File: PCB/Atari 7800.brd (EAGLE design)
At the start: 58.5 x 61 mm, 28 parts, among them U1A SN74AHCT125N, U2A SN74AHCT125N, U3A SN74AHCT125N, U4 CD74HC4053E, U5 CD74HC4053E

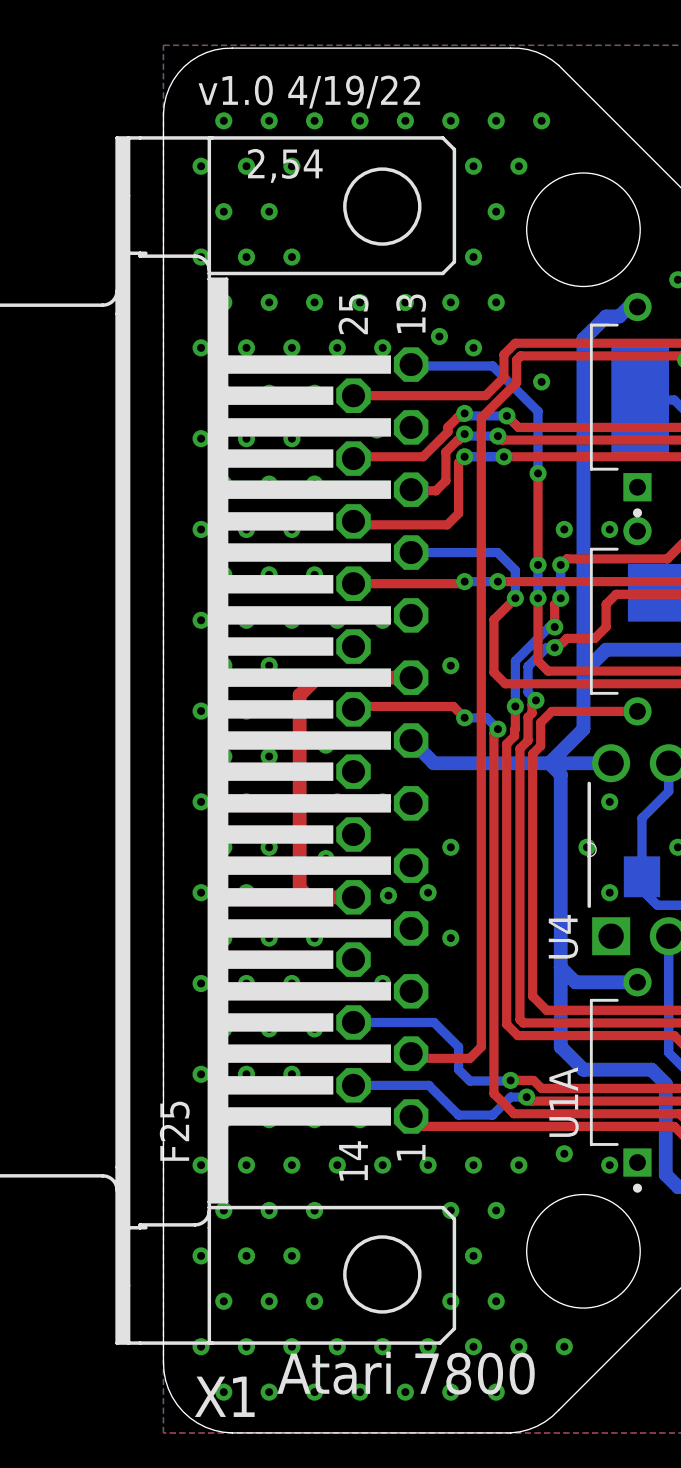
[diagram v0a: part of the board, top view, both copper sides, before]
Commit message: Added exposed GND plane at DB25 anchors
All PCBs have been update to have exposed GND plane pads for the DB25 anchor points.

This resolves Issue 54
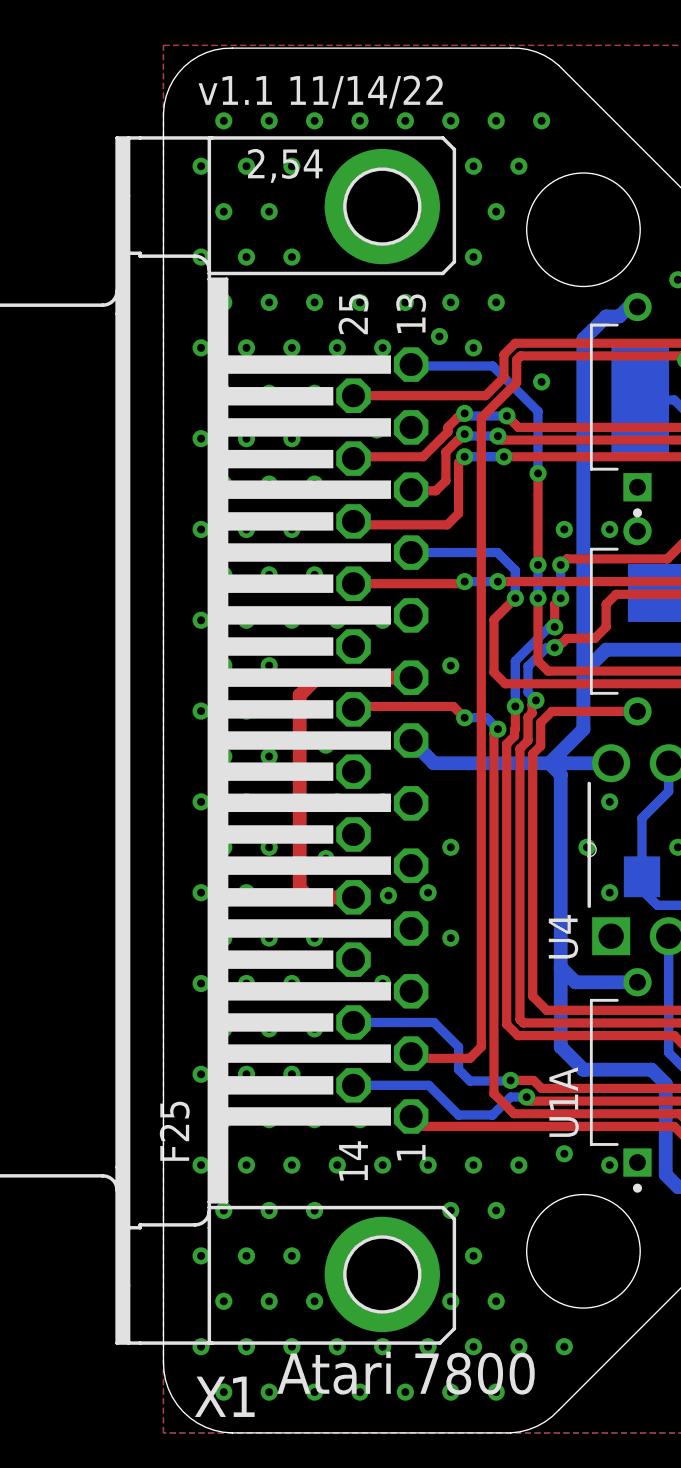
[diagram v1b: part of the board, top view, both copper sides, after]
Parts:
- X1: device SparkFun-Retired:F25H -> SparkFun-Retired:F25HP
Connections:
- net GND: now also X1.GND1, X1.GND2
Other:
- board text added: "v1.1 11/14/22"
- board text removed: "v1.0 4/19/22"
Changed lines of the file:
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@@
 <drawing>
 <settings>
-<setting alwaysvectorfont="yes"/>
+<setting alwaysvectorfont="no"/>
 <setting verticaltext="up"/>
 </settings>
@@
 <hole x="18.5" y="53" drill="5"/>
 <hole x="18.5" y="8" drill="5"/>
-<text x="1.5" y="58.5" size="1.27" layer="21">v1.0 4/19/22</text>
+<text x="1.5" y="58.5" size="1.27" layer="21">v1.1 11/14/22</text>
 <text x="16.5" y="3.5" size="1.778" layer="21" rot="R180">Atari 7800</text>
 <wire x1="58.5" y1="46.377359375" x2="58.5" y2="43.5" width="0" layer="20"/>
@@
 <attribute name="PURCHASE-URL" value="https://pricing.snapeda.com/search/part/SN74AHCT125N/?ref=eda" x="149.15" y="56.521" size="1.778" layer="27" rot="R90" display="off"/>
 </element>
-<element name="X1" library="SparkFun-Retired" package="F25H" value="" x="9.64" y="30.5" smashed="yes" rot="R90">
+<element name="X1" library="SparkFun-Retired" package="F25HP" value="" x="9.64" y="30.5" smashed="yes" rot="R90">
 <attribute name="NAME" x="4.219" y="2.48" size="1.778" layer="25" ratio="10" rot="R180"/>
 <attribute name="VALUE" x="-4.33" y="22.118" size="1.778" layer="27" ratio="10" rot="R90"/>
@@
 <contactref element="U2A" pad="13"/>
 <contactref element="U2A" pad="1"/>
-<contactref element="X1" pad="3"/>
-<contactref element="X1" pad="6"/>
-<contactref element="X1" pad="5"/>
-<contactref element="X1" pad="4"/>
-<contactref element="X1" pad="9"/>
 <contactref element="GND1" pad="1"/>
 <contactref element="GND2" pad="1"/>
-<contactref element="X1" pad="16"/>
 <contactref element="U4" pad="7"/>
 <contactref element="U4" pad="8"/>
@@
 <via x="54.6568" y="17.7968" extent="1-16" drill="0.35"/>
 <via x="56.6568" y="17.7968" extent="1-16" drill="0.35"/>
+<contactref element="X1" pad="3"/>
+<contactref element="X1" pad="6"/>
+<contactref element="X1" pad="5"/>
+<contactref element="X1" pad="4"/>
+<contactref element="X1" pad="9"/>
+<contactref element="X1" pad="16"/>
+<contactref element="X1" pad="GND2"/>
+<contactref element="X1" pad="GND1"/>
 </signal>
 <signal name="5VIN">

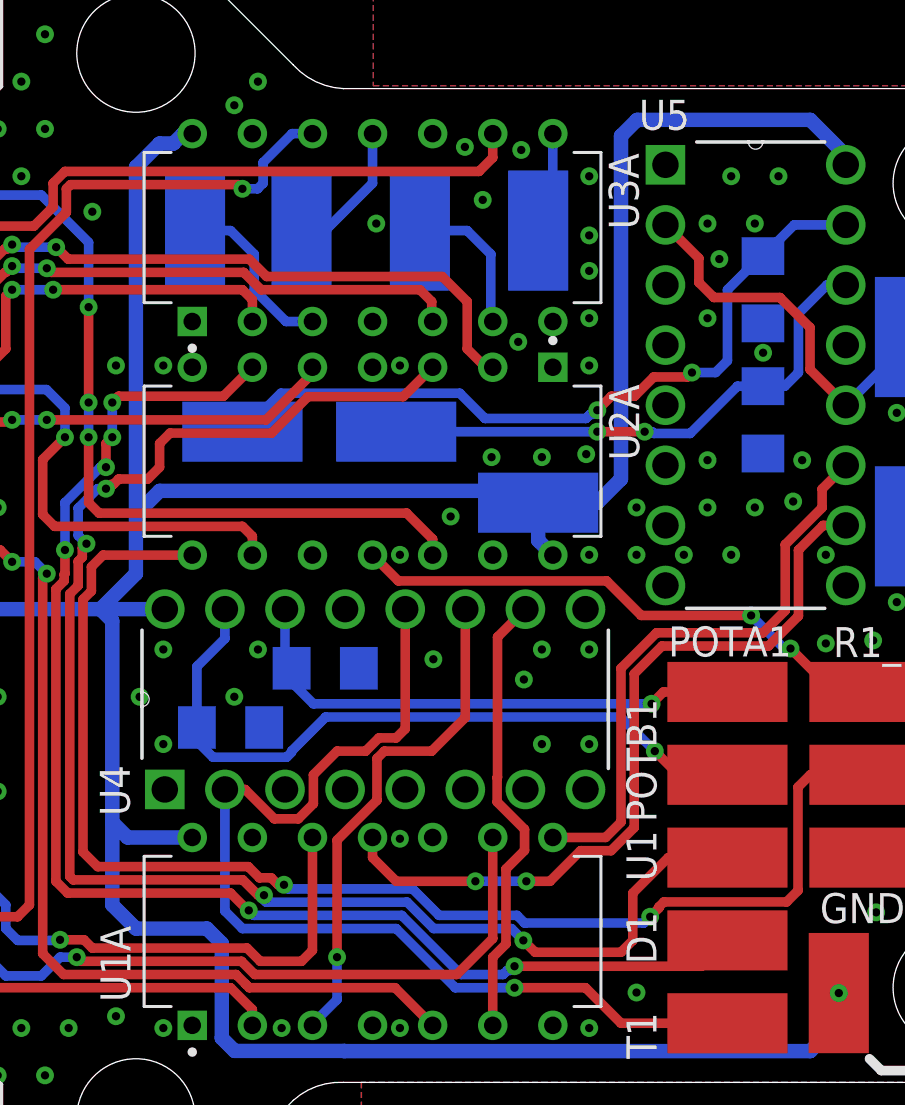
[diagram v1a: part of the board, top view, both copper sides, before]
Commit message: Silkscreen Update, Library Add, Datasheet Add
Updated the silkscreen on all PCBs that used the SN74 components as there was not orientation marker on the silkscreen.

Added Modified SN74 libraries and VB Cable Pinout image
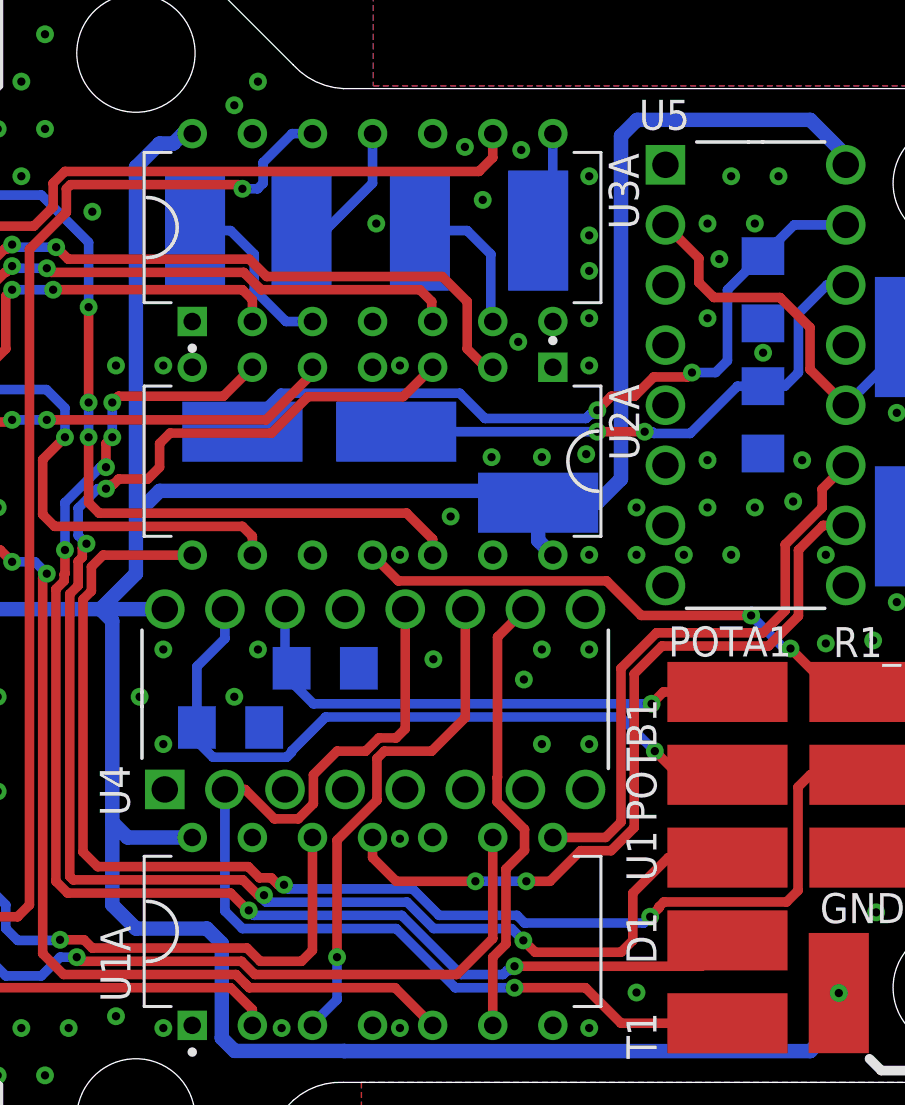
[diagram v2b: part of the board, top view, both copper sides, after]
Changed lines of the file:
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@@
 <drawing>
 <settings>
-<setting alwaysvectorfont="no"/>
+<setting alwaysvectorfont="yes"/>
 <setting verticaltext="up"/>
 </settings>
